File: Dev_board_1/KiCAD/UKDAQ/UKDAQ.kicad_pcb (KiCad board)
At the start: 2 copper layers, 73.2 x 56.9 mm, 24 parts, among them J1 5 pin Molex (0537800570), J2 Conn_01x11_Male, U1 AP2210N_SOT-23-3, U2 PI4ULS5V202, U3 BNO055, U4 BME280, U5 MAX32660-20TQFN-EP, Y1 Crystal

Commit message: Havent pushed in a while. Dev board is now baseline functional
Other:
- board text added: "LA-UKDAQ-rev_0.8-8/10/23"
- board text removed: "LA-UKDAQ-rev_0.5-6/21/23"

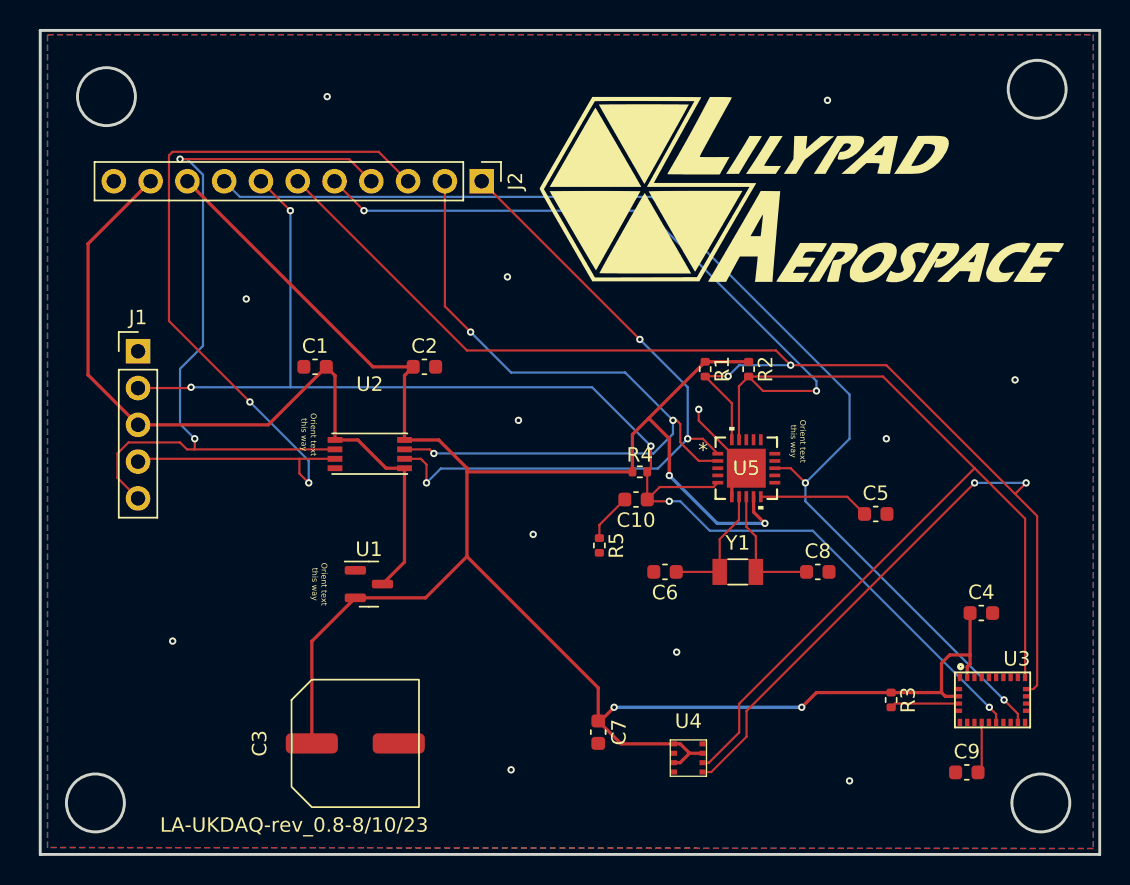
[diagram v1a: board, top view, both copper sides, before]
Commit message: Shrunk size of the dev board significantly
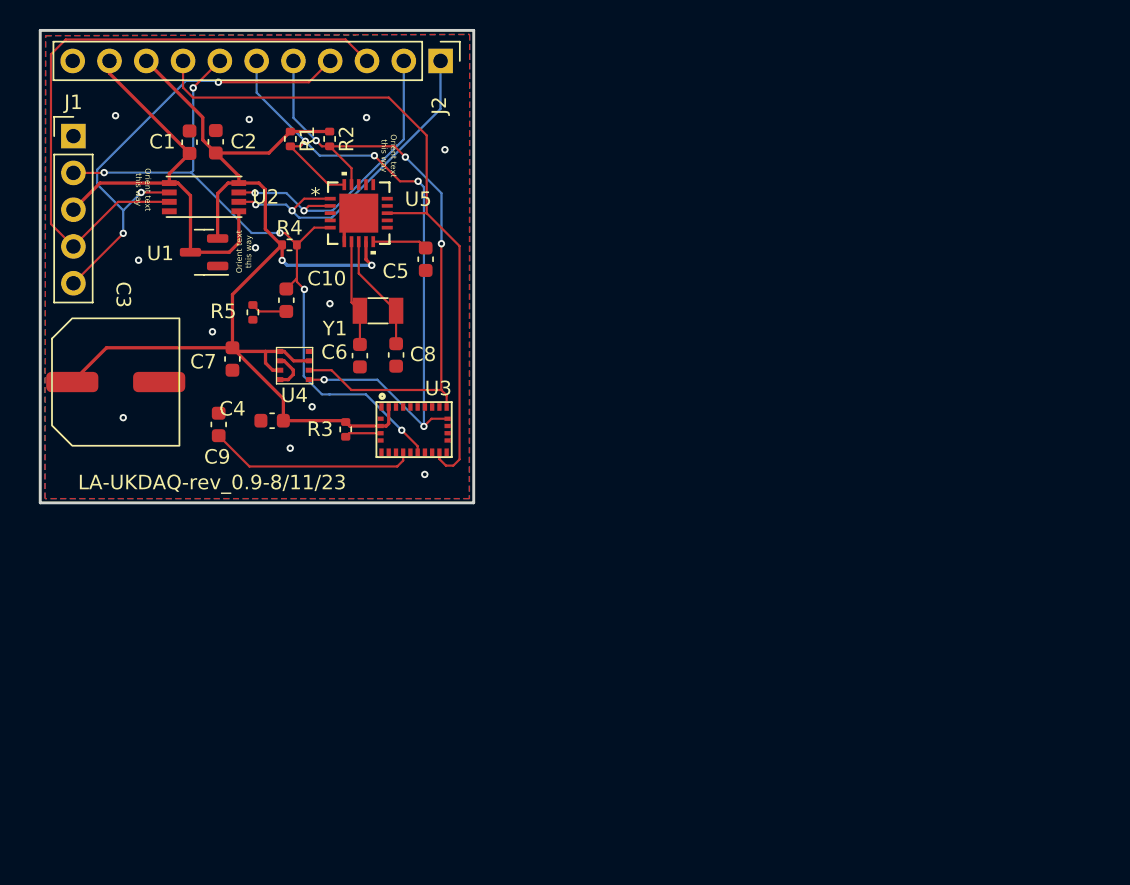
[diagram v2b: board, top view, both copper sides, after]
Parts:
- removed G***: LOGO, Joseph:LilypadAerospace_3mm
- moved C9 57.0 mm to (91.6, 108.0), turned to -90 degrees
- moved C4 50.7 mm to (95.3, 107.7), turned to 180 degrees
- moved U3 44.1 mm to (105.1, 108.3)
- moved R3 42.0 mm to (100.3, 108.3)
- moved U4 38.4 mm to (96.8, 103.9)
- moved C7 36.1 mm to (92.5, 103.5)
- moved C5 35.7 mm to (105.9, 96.6), turned to -90 degrees
- moved R2 33.0 mm to (99.2, 88.3)
- moved R1 32.8 mm to (96.5, 88.3)
- moved C8 32.7 mm to (103.8, 103.2), turned to -90 degrees
- moved U5 32.0 mm to (101.2, 93.4)
- moved Y1 30.7 mm to (102.6, 100.1)
- moved C3 29.9 mm to (84.5, 105.0)
- moved R5 28.8 mm to (93.9, 100.2)
- moved R4 28.8 mm to (96.5, 95.6)
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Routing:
- net VDD: track 155.6 -> 83.3 mm, vias 4 -> 2
- net /SDA: track 111.8 -> 44.2 mm, vias 2 -> 3
- net /SCL: track 117.2 -> 50.0 mm, vias 4 -> 5
- net /nRESET: track 92.1 -> 49.4 mm
- net /BNO_INTERRUPT: track 81.8 -> 48.3 mm, vias 2 -> 0
- net /TX/SWDIO-VDD: track 52.8 -> 21.3 mm, vias 3 -> 2
- net /RX/SWCLK-VDD: track 48.4 -> 23.8 mm, vias 3 -> 2
- net VCC: track 54.2 -> 30.2 mm
- net /TX/SWDIO-VCC: track 55.1 -> 33.0 mm, vias 2 -> 3
- net /RX/SWCLK-VCC: track 59.7 -> 44.7 mm, vias 2 -> 0
- net Net-(C9-Pad2): track 3.54 -> 14.4 mm
- net Net-(C5-Pad1): track 7.65 -> 3.80 mm
- net GND: track 7.81 -> 4.98 mm, vias 13 -> 12
- net Net-(R3-Pad2): track 4.80 -> 2.51 mm
- net Net-(C6-Pad1): track 8.75 -> 7.34 mm
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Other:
- board size 73.2 x 56.9 mm -> 29.9 x 32.6 mm
- board text added: "LA-UKDAQ-rev_0.9-8/11/23"
- board text removed: "LA-UKDAQ-rev_0.8-8/10/23"
